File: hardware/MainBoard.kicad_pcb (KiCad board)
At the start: 2 copper layers, 50 x 50 mm, 12 parts, among them P1 CONN_01X07, P2 CONN_01X04, P3 CONN_01X04, P4 CONN_01X07, P5 ON/OFF, P6 BATTERY, U1 4056_CARG

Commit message: Clean PCB
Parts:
- removed D1: D, Diodes_ThroughHole:Diode_DO-41_SOD81_Horizontal_RM10
- removed P5: ON/OFF, Pin_Headers:Pin_Header_Straight_1x02
- removed P6: BATTERY, Pin_Headers:Pin_Header_Straight_1x02
- removed RAW1: ARDUPROMINI, arduinoMiniPro
- removed U1: 4056_CARG, 4056_lipoCharg
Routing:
- net +BATT: track 137.4 -> 0.00 mm, vias 1 -> 0
- net GND: track 83.5 -> 0.00 mm, vias 2 -> 0
- net Net-(D1-Pad2): track 55.6 -> 0.00 mm
- net /RST: track 44.9 -> 0.00 mm
- net /A3: track 40.7 -> 0.00 mm
- net /A1: track 39.8 -> 0.00 mm
- net /A2: track 38.3 -> 0.00 mm
- net /A0: track 35.0 -> 0.00 mm
- net /SCK: track 27.9 -> 0.00 mm
- net /DHT/D6: track 26.0 -> 0.00 mm
- net /NSS: track 25.1 -> 0.00 mm, vias 1 -> 0
- net /MISO: track 24.4 -> 0.00 mm
- net /SDA: track 24.3 -> 0.00 mm
- net /MOSI: track 23.8 -> 0.00 mm, vias 1 -> 0
- net /INT0: track 20.1 -> 0.00 mm
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- removed copper zone on B.Cu, net GND
- removed copper zone on F.Cu, net GND
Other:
- board text added: "CaTSat Zero"
- board text removed: "+"
- board text removed: "CaTSat 1.1v"

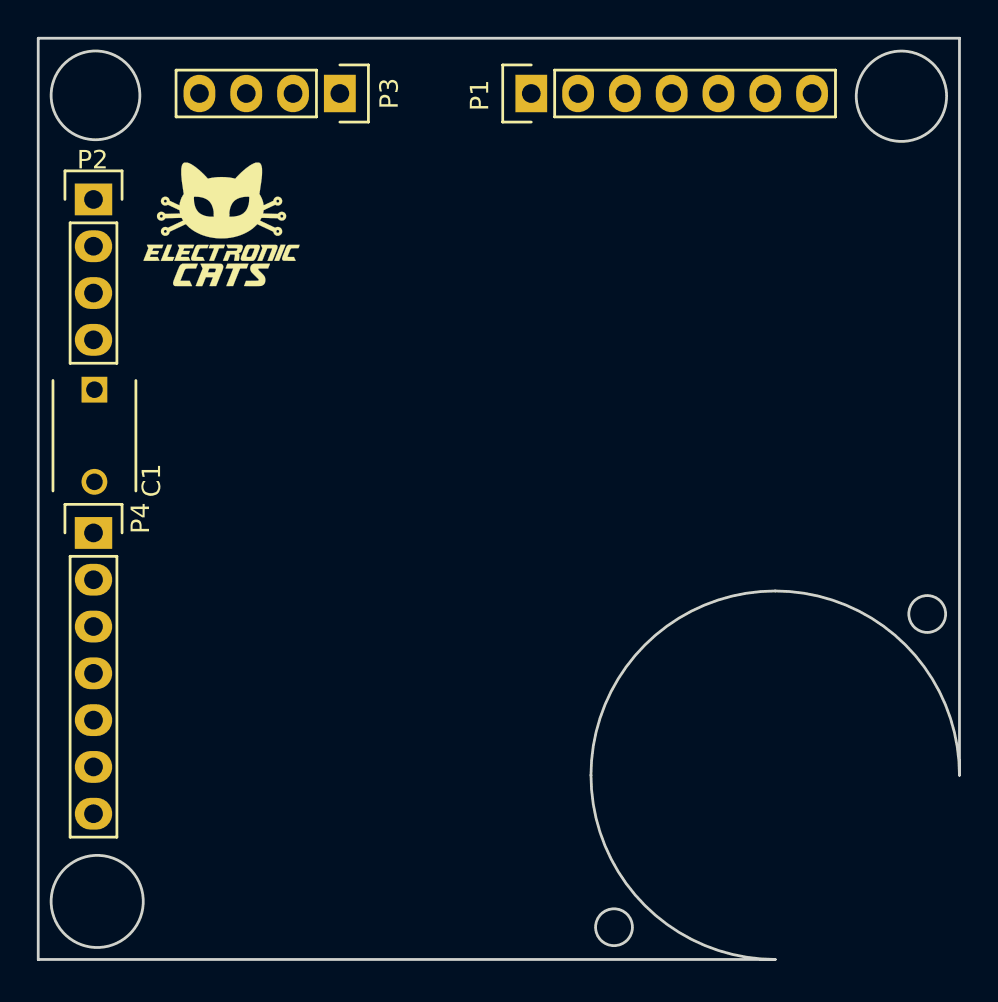
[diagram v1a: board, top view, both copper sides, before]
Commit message: Update PCB battery Hole
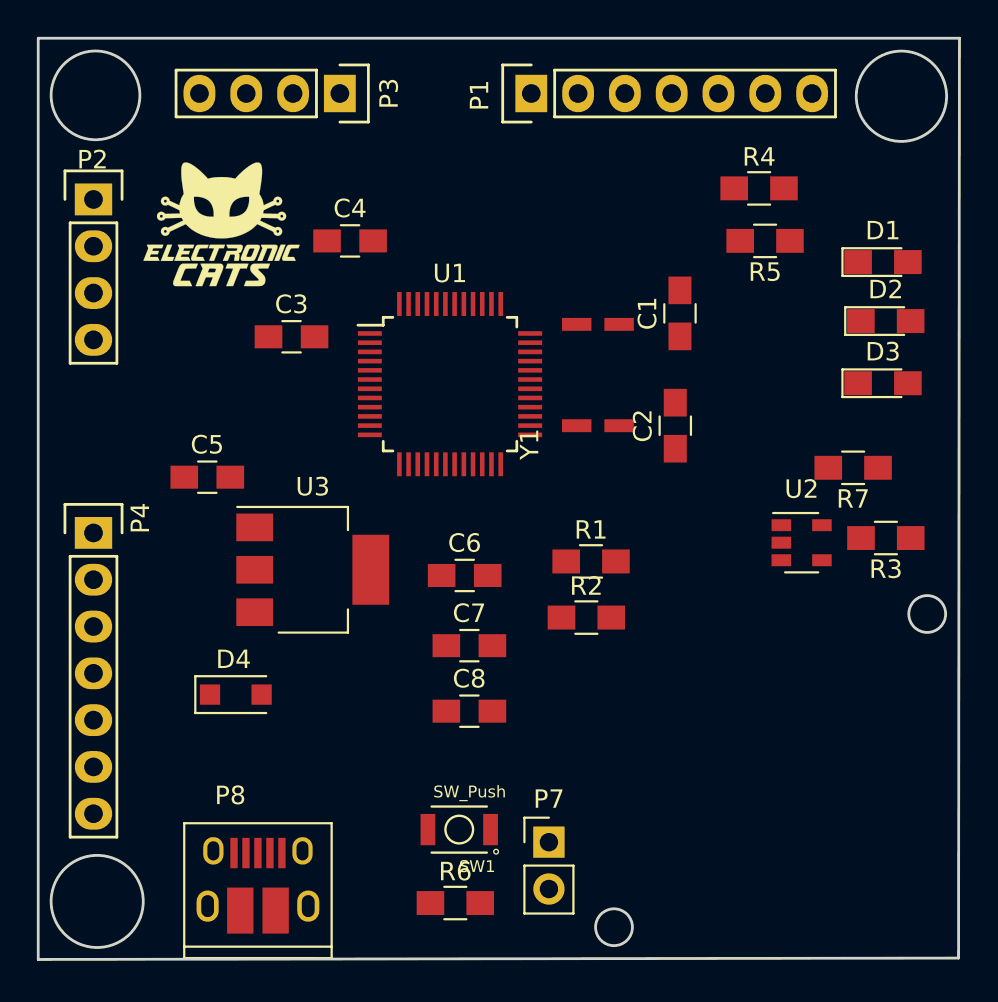
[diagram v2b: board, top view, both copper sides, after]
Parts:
- added C2: 22pF, Capacitors_SMD:C_0805_HandSoldering, F.Cu at (119.1, 74.9)
- added C3: 1uF, Capacitors_SMD:C_0805_HandSoldering, F.Cu at (98.3, 70.1)
- added C4: 1uF, Capacitors_SMD:C_0805_HandSoldering, F.Cu at (101.5, 64.9)
- added C5: 10uF, Capacitors_SMD:C_0805_HandSoldering, F.Cu at (93.7, 77.7)
- added C6: 10uF, Capacitors_SMD:C_0805_HandSoldering, F.Cu at (107.7, 83.1)
- added C7: 0.1uF, Capacitors_SMD:C_0805_HandSoldering, F.Cu at (108.0, 86.9)
- added C8: 0.1uF, Capacitors_SMD:C_0805_HandSoldering, F.Cu at (108.0, 90.4)
- added D1: LED, LEDs:LED_0805_HandSoldering, F.Cu at (130.4, 66.0)
- added D2: LED, LEDs:LED_0805_HandSoldering, F.Cu at (130.6, 69.2)
- added D3: LED, LEDs:LED_0805_HandSoldering, F.Cu at (130.4, 72.6)
- added D4: MBR120, Diodes_SMD:D_SOD-123F, F.Cu at (95.3, 89.5)
- added P7: CONN_01X02, Pin_Headers:Pin_Header_Straight_1x02_Pitch2.54mm, F.Cu at (112.3, 97.5)
- added P8: USB_Micro, Connect:USB_Micro-B_10103594-0001LF, F.Cu at (96.5, 99.6)
- added R1: 100k, Resistors_SMD:R_0805_HandSoldering, F.Cu at (114.6, 82.3)
- added R2: 100k, Resistors_SMD:R_0805_HandSoldering, F.Cu at (114.3, 85.3)
- added R3: 10k, Resistors_SMD:R_0805_HandSoldering, F.Cu at (130.6, 81.0)
- added R4: 1K, Resistors_SMD:R_0805_HandSoldering, F.Cu at (123.7, 62.0)
- added R5: 1K, Resistors_SMD:R_0805_HandSoldering, F.Cu at (124.0, 64.9)
- added R6: 10k, Resistors_SMD:R_0805_HandSoldering, F.Cu at (107.2, 100.8)
- added R7: 330, Resistors_SMD:R_0805_HandSoldering, F.Cu at (128.8, 77.2)
- added SW1: SW_Push, TIH:SW_B3U-1000P, F.Cu at (107.4, 96.8)
- added U1: ATSAMD21G18A-AU, Housings_QFP:TQFP-48_7x7mm_Pitch0.5mm, F.Cu at (106.9, 72.7)
- added U2: MCP73831T-2ACI/OT, TO_SOT_Packages_SMD:SOT-23-5, F.Cu at (126.0, 81.3)
- added U3: AP2114, TO_SOT_Packages_SMD:SOT-223-3_TabPin2, F.Cu at (99.5, 82.8)
- added Y1: 32.768, TIH:LFXTAL016178Reel, F.Cu at (116.1, 74.9)
- C1: value 0.1uF -> 22pF; footprint Capacitors_ThroughHole:C_Disc_D6_P5 -> Capacitors_SMD:C_0805_HandSoldering
- moved C1 32.0 mm to (119.4, 68.8), turned to 90 degrees
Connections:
- C1 pad 1: +BATT -> GND
- C1 pad 2: GND -> Net-(C1-Pad2)
- P3 pad 1: /INT0 -> /A5/INT2
- P3 pad 2: /INT1 -> /A4/INT5
- P3 pad 4: /D8 -> /D5
- P4 pad 7: /RST -> /RFM_RST
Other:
- outline, holes or cut-outs redrawn
- board text added: "RX2 TX2"
- board text removed: "S_RX S_TX"

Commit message: Update for MakeCode
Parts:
- removed P7: CONN_01X02, Pin_Headers:Pin_Header_Straight_1x02_Pitch2.54mm
- removed R6: 10k, Resistors_SMD:R_0805_HandSoldering
- removed SW1: SW_Push, TIH:SW_B3U-1000P
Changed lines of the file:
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@@
-(kicad_pcb (version 4) (host pcbnew 4.0.7)
+(kicad_pcb (version 20171130) (host pcbnew "(5.0.0-3-g5ebb6b6)")
   (general
-    (links 81)
-    (no_connects 81)
-    (area 73.537672 42.45 152.328572 110.100001)
     (thickness 1.6)
     (drawings 39)
     (tracks 3)
     (zones 0)
-    (modules 32)
+    (modules 29)
     (nets 54)
   )
@@
       (layerselection 0x010f0_80000001)
       (usegerberextensions false)
+      (usegerberattributes false)
+      (usegerberadvancedattributes false)
+      (creategerberjobfile false)
       (excludeedgelayer true)
       (linewidth 0.100000)
@@
       (hpglpennumber 1)
       (hpglpenspeed 20)
-      (hpglpendiameter 15)
-      (hpglpenoverlay 2)
+      (hpglpendiameter 15.000000)
       (psnegative false)
       (psa4output false)
@@
       (drillshape 0)
       (scaleselection 1)
-      (outputdirectory Produccion/CatSatMain/))
+      (outputdirectory "Produccion/CatSatMain/"))
   )
   (net 0 "")
@@
       (net 7 /DHT/D6))
     (model Pin_Headers.3dshapes/Pin_Header_Straight_1x07.wrl
-      (at (xyz 0 -0.3 0))
+      (offset (xyz 0 -7.619999885559082 0))
       (scale (xyz 1 1 1))
       (rotate (xyz 0 0 90))
@@
       (net 11 /A0))
     (model Pin_Headers.3dshapes/Pin_Header_Straight_1x04.wrl
-      (at (xyz 0 -0.15 0))
+      (offset (xyz 0 -3.809999942779541 0))
       (scale (xyz 1 1 1))
       (rotate (xyz 0 0 90))
@@
       (net 29 /RFM_RST))
     (model Pin_Headers.3dshapes/Pin_Header_Straight_1x07.wrl
-      (at (xyz 0 -0.3 0))
+      (offset (xyz 0 -7.619999885559082 0))
       (scale (xyz 1 1 1))
       (rotate (xyz 0 0 90))
@@
       (effects (font (size 1 1) (thickness 0.15)))
     )
-    (fp_text value CONN_01X04 (at -2.25 4.83 360) (layer F.Fab)
+    (fp_text value CONN_01X04 (at -2.25 4.83) (layer F.Fab)
       (effects (font (size 1 1) (thickness 0.15)))
     )
@@
       (net 28 /D5))
     (model Pin_Headers.3dshapes/Pin_Header_Straight_1x04.wrl
-      (at (xyz 0 -0.15 0))
+      (offset (xyz 0 -3.809999942779541 0))
       (scale (xyz 1 1 1))
       (rotate (xyz 0 0 90))
@@
     (at 94.5 64)
     (fp_text reference G*** (at 0 0) (layer F.SilkS) hide
-      (effects (font (thickness 0.3)))
+      (effects (font (size 1.524 1.524) (thickness 0.3)))
     )
     (fp_text value LOGO (at 0.75 0) (layer F.SilkS) hide
-      (effects (font (thickness 0.3)))
+      (effects (font (size 1.524 1.524) (thickness 0.3)))
     )
     (fp_poly (pts (xy -1.511952 2.134469) (xy -1.457322 2.134584) (xy -1.408721 2.134798) (xy -1.367028 2.135106)
@@
     )
   )
-  (module Pin_Headers:Pin_Header_Straight_1x02_Pitch2.54mm (layer F.Cu)
-    (at 112.268 97.536)
-    (descr "Through hole straight pin header, 1x02, 2.54mm pitch, single row")
-    (tags "Through hole pin header THT 1x02 2.54mm single row")
-    (fp_text reference P7 (at 0 -2.33) (layer F.SilkS)
-      (effects (font (size 1 1) (thickness 0.15)))
-    )
-    (fp_text value CONN_01X02 (at 0 4.87) (layer F.Fab)
-      (effects (font (size 1 1) (thickness 0.15)))
-    )
-    (fp_line (start -0.635 -1.27) (end 1.27 -1.27) (layer F.Fab) (width 0.1))
-    (fp_line (start 1.27 -1.27) (end 1.27 3.81) (layer F.Fab) (width 0.1))
-    (fp_line (start 1.27 3.81) (end -1.27 3.81) (layer F.Fab) (width 0.1))
-    (fp_line (start -1.27 3.81) (end -1.27 -0.635) (layer F.Fab) (width 0.1))
-    (fp_line (start -1.27 -0.635) (end -0.635 -1.27) (layer F.Fab) (width 0.1))
-    (fp_line (start -1.33 3.87) (end 1.33 3.87) (layer F.SilkS) (width 0.12))
-    (fp_line (start -1.33 1.27) (end -1.33 3.87) (layer F.SilkS) (width 0.12))
-    (fp_line (start 1.33 1.27) (end 1.33 3.87) (layer F.SilkS) (width 0.12))
-    (fp_line (start -1.33 1.27) (end 1.33 1.27) (layer F.SilkS) (width 0.12))
-    (fp_line (start -1.33 0) (end -1.33 -1.33) (layer F.SilkS) (width 0.12))
-    (fp_line (start -1.33 -1.33) (end 0 -1.33) (layer F.SilkS) (width 0.12))
-    (fp_line (start -1.8 -1.8) (end -1.8 4.35) (layer F.CrtYd) (width 0.05))
-    (fp_line (start -1.8 4.35) (end 1.8 4.35) (layer F.CrtYd) (width 0.05))
-    (fp_line (start 1.8 4.35) (end 1.8 -1.8) (layer F.CrtYd) (width 0.05))
-    (fp_line (start 1.8 -1.8) (end -1.8 -1.8) (layer F.CrtYd) (width 0.05))
-    (fp_text user %R (at 0 1.27 90) (layer F.Fab)
-      (effects (font (size 1 1) (thickness 0.15)))
-    )
-    (pad 1 thru_hole rect (at 0 0) (size 1.7 1.7) (drill 1) (layers *.Cu *.Mask)
-      (net 30 /SWDIO))
-    (pad 2 thru_hole oval (at 0 2.54) (size 1.7 1.7) (drill 1) (layers *.Cu *.Mask)
-      (net 31 /SWCLK))
-    (model ${KISYS3DMOD}/Pin_Headers.3dshapes/Pin_Header_Straight_1x02_Pitch2.54mm.wrl
-      (at (xyz 0 0 0))
-      (scale (xyz 1 1 1))
-      (rotate (xyz 0 0 0))
-    )
-  )
   (module Connect:USB_Micro-B_10103594-0001LF (layer F.Cu)
     (at 96.475 99.625)
@@
   )
   (module Resistors_SMD:R_0805_HandSoldering (layer F.Cu)
-    (at 107.188 100.838)
-    (descr "Resistor SMD 0805, hand soldering")
-    (tags "resistor 0805")
-    (attr smd)
-    (fp_text reference R6 (at 0 -1.7) (layer F.SilkS)
-      (effects (font (size 1 1) (thickness 0.15)))
-    )
-    (fp_text value 10k (at 0 1.75) (layer F.Fab)
-      (effects (font (size 1 1) (thickness 0.15)))
-    )
-    (fp_text user %R (at 0 0) (layer F.Fab)
-      (effects (font (size 0.5 0.5) (thickness 0.075)))
-    )
-    (fp_line (start -1 0.62) (end -1 -0.62) (layer F.Fab) (width 0.1))
-    (fp_line (start 1 0.62) (end -1 0.62) (layer F.Fab) (width 0.1))
-    (fp_line (start 1 -0.62) (end 1 0.62) (layer F.Fab) (width 0.1))
-    (fp_line (start -1 -0.62) (end 1 -0.62) (layer F.Fab) (width 0.1))
-    (fp_line (start 0.6 0.88) (end -0.6 0.88) (layer F.SilkS) (width 0.12))
-    (fp_line (start -0.6 -0.88) (end 0.6 -0.88) (layer F.SilkS) (width 0.12))
-    (fp_line (start -2.35 -0.9) (end 2.35 -0.9) (layer F.CrtYd) (width 0.05))
-    (fp_line (start -2.35 -0.9) (end -2.35 0.9) (layer F.CrtYd) (width 0.05))
-    (fp_line (start 2.35 0.9) (end 2.35 -0.9) (layer F.CrtYd) (width 0.05))
-    (fp_line (start 2.35 0.9) (end -2.35 0.9) (layer F.CrtYd) (width 0.05))
-    (pad 1 smd rect (at -1.35 0) (size 1.5 1.3) (layers F.Cu F.Paste F.Mask)
-      (net 41 /RESET))
-    (pad 2 smd rect (at 1.35 0) (size 1.5 1.3) (layers F.Cu F.Paste F.Mask)
-      (net 22 +3V3))
-    (model ${KISYS3DMOD}/Resistors_SMD.3dshapes/R_0805.wrl
-      (at (xyz 0 0 0))
-      (scale (xyz 1 1 1))
-      (rotate (xyz 0 0 0))
-    )
-  )
-  (module Resistors_SMD:R_0805_HandSoldering (layer F.Cu)
     (at 128.778 77.216 180)
     (descr "Resistor SMD 0805, hand soldering")
@@
     )
   )
-  (module TIH:SW_B3U-1000P (layer F.Cu)
-    (at 107.4 96.85 180)
-    (solder_mask_margin 0.1)
-    (attr smd)
-    (fp_text reference SW1 (at -0.9744 -2.0064 180) (layer F.SilkS)
-      (effects (font (size 0.64 0.64) (thickness 0.05)))
-    )
-    (fp_text value SW_Push (at -0.568 2.0436 180) (layer F.SilkS)
-      (effects (font (size 0.64 0.64) (thickness 0.05)))
-    )
-    (fp_line (start 1.5 -1.25) (end -1.5 -1.25) (layer F.SilkS) (width 0.127))
-    (fp_line (start -1.5 -1.25) (end -1.5 1.25) (layer Dwgs.User) (width 0.127))
-    (fp_line (start -1.5 1.25) (end 1.5 1.25) (layer F.SilkS) (width 0.127))
-    (fp_line (start 1.5 1.25) (end 1.5 -1.25) (layer Dwgs.User) (width 0.127))
-    (fp_circle (center -2 -1.2) (end -1.873 -1.2) (layer F.SilkS) (width 0))
-    (fp_line (start 2.5 1.45) (end -2.5 1.45) (layer Dwgs.User) (width 0.127))
-    (fp_line (start -2.5 1.45) (end -2.5 -1.5) (layer Dwgs.User) (width 0.127))
-    (fp_line (start -2.5 -1.5) (end 2.5 -1.5) (layer Dwgs.User) (width 0.127))
-    (fp_line (start 2.5 -1.5) (end 2.5 1.45) (layer Dwgs.User) (width 0.127))
-    (fp_circle (center 0 0) (end 0.75 0) (layer F.SilkS) (width 0.127))
-    (pad 2 smd rect (at 1.7 0) (size 0.8 1.7) (layers F.Cu F.Paste F.Mask)
-      (net 41 /RESET) (solder_mask_margin 0.2))
-    (pad 1 smd rect (at -1.7 0) (size 0.8 1.7) (layers F.Cu F.Paste F.Mask)
-      (net 1 GND) (solder_mask_margin 0.2))
-  )
   (module Housings_QFP:TQFP-48_7x7mm_Pitch0.5mm (layer F.Cu)
